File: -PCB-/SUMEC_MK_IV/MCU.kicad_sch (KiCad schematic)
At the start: 24 parts, among them J13 USB_TypeC, SW2 SW_Push, SW3 SW_Push, SW4 SW_Push, SW5 SW_Push, U3 ESP32-S3-WROOM-1, U4 USBLC6-2SC6

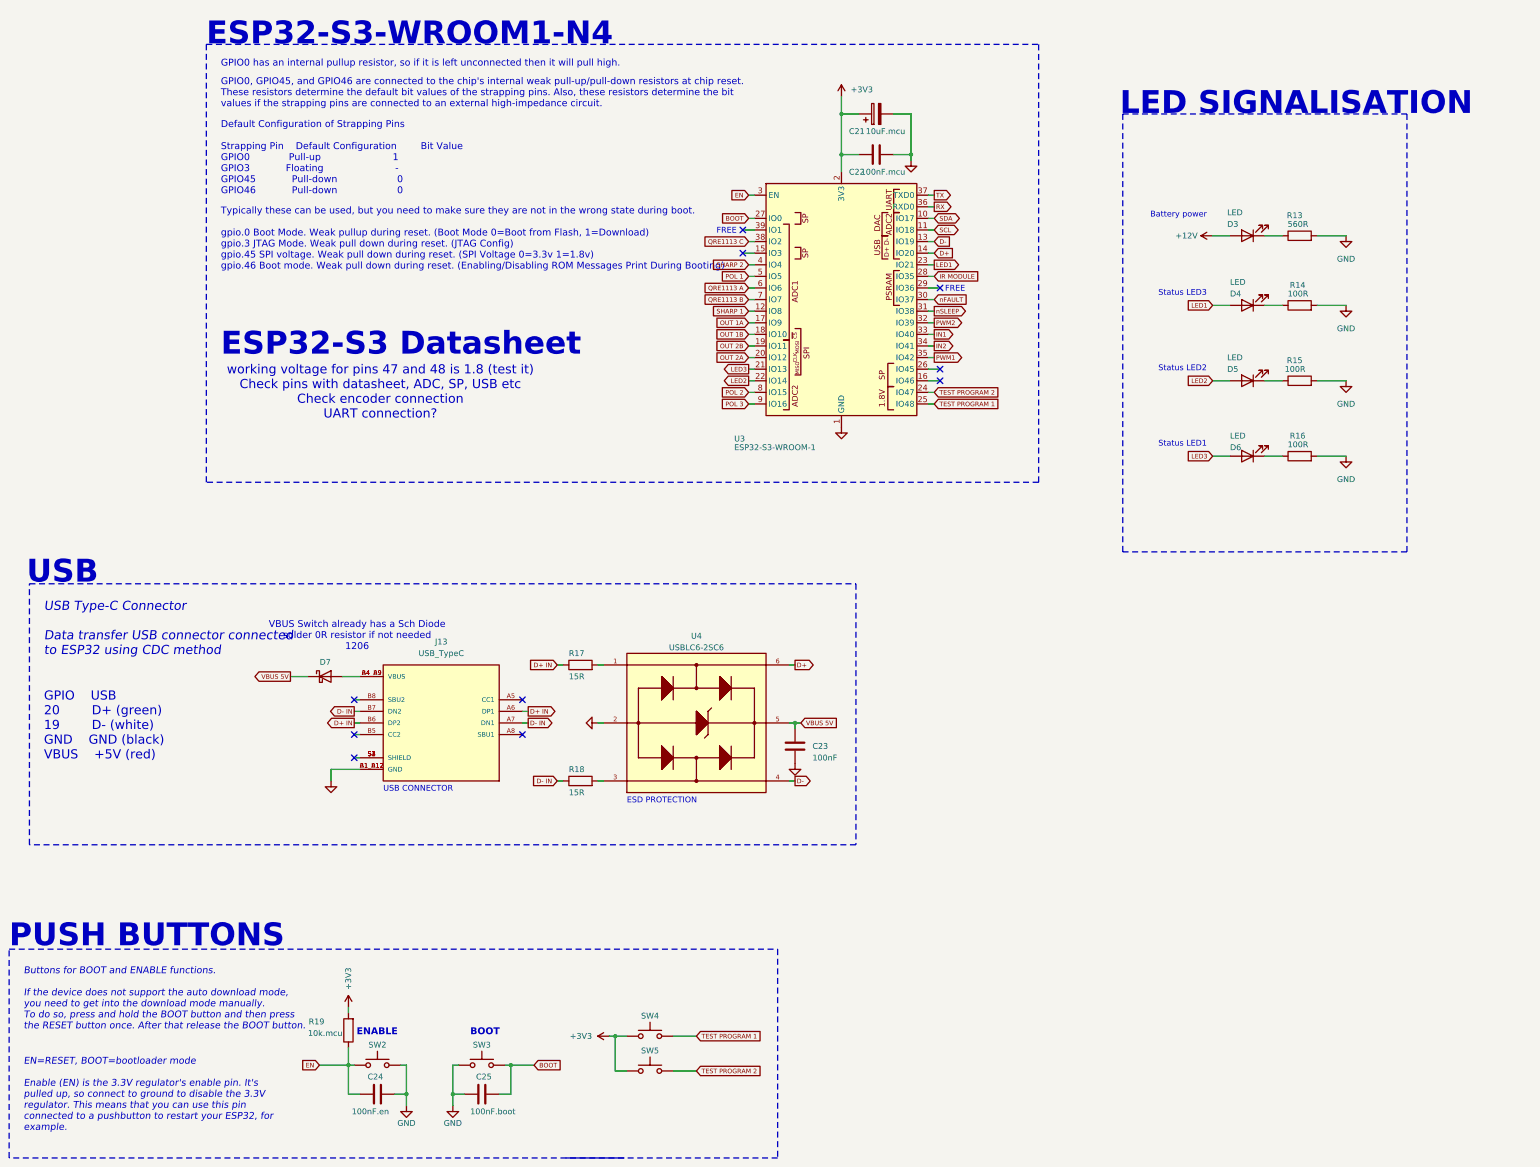
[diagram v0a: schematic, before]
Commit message: Schematic and PCB update
Schematic update:
- Font adjustment
- Block rearrangement

PCB update
- Silkscreen
- Minor layout update
- Graphic update
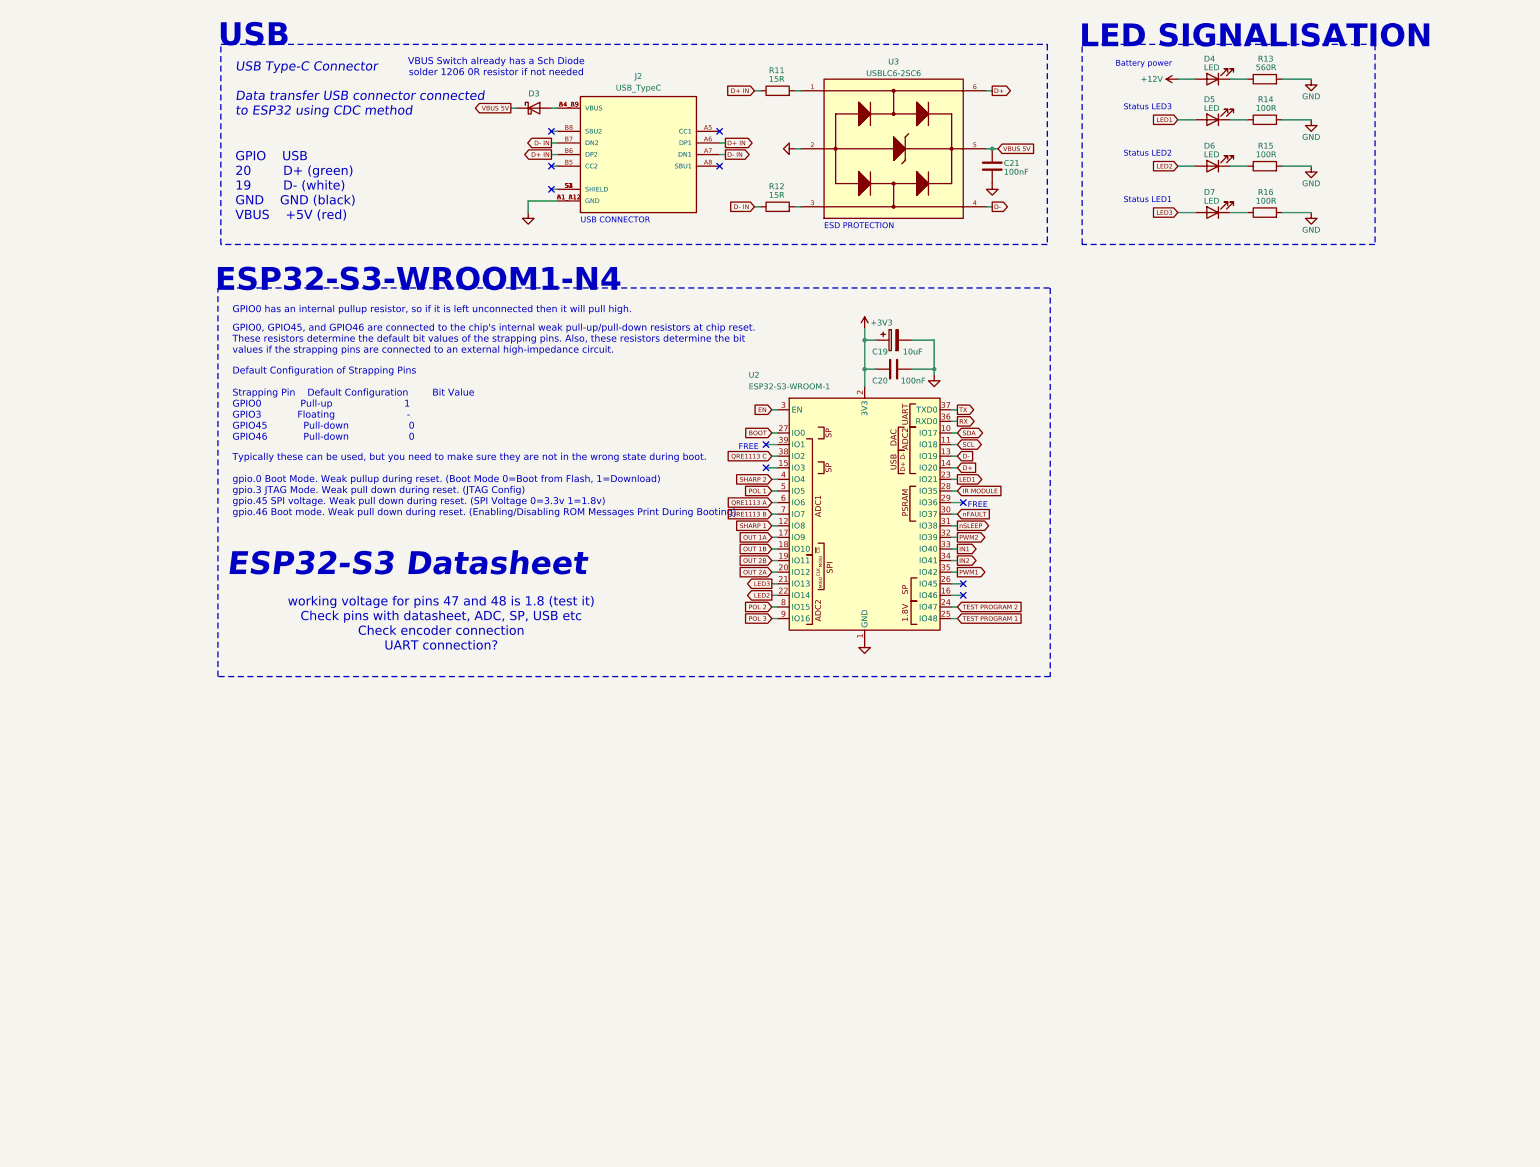
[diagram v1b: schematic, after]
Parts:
- removed C24: 100nF.en, Capacitor_SMD:C_0805_2012Metric_Pad1.18x1.45mm_HandSolder, symbol Device:C
- removed C25: 100nF.boot, Capacitor_SMD:C_0805_2012Metric_Pad1.18x1.45mm_HandSolder, symbol Device:C
- removed R19: 10k.mcu, Resistor_SMD:R_0805_2012Metric_Pad1.20x1.40mm_HandSolder, symbol Device:R
- removed SW2, SW3, SW4, SW5: SW_Push, Button_Switch_SMD:SW_SPST_EVQPE1, symbol Switch:SW_Push
- removed U3: ESP32-S3-WROOM-1, PCM_Espressif:ESP32-S3-WROOM-1, symbol sumec_sch_lib:ESP32-S3-WROOM-1_CUSTOM_made_by_bismarx
- added U2: ESP32-S3-WROOM-1, PCM_Espressif:ESP32-S3-WROOM-1, symbol sumec_sch_lib:ESP32-S3-WROOM-1_CUSTOM_made_by_bismarx
- C19: renamed from C21; value 10uF.mcu -> 10uF
- C20: renamed from C22; value 100nF.mcu -> 100nF
- renumbered C23 to C21, D7 to D3, D3 to D4, D4 to D5, D5 to D6, D6 to D7, J13 to J2, R17 to R11, R18 to R12, U4 to U3
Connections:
- net +3V3: now also U2.2 (3V3)
- net BOOT: now also U2.27 (IO0)
- net D+: now also U2.14 (IO20)
- net D-: now also U2.13 (IO19)
- net EN: now also U2.3 (EN)
- net GND: now also U2.1 (GND), U2.40 (GND), U2.41 (GND)
- net IN1: now also U2.33 (IO40)
- net IN2: now also U2.34 (IO41)
- net IR MODULE: now also U2.28 (IO35)
- net LED1: now also U2.23 (IO21)
- net LED2: now also U2.22 (IO14)
- net LED3: now also U2.21 (IO13)
- net OUT 1A: now also U2.17 (IO9)
- net OUT 1B: now also U2.18 (IO10)
- net OUT 2A: now also U2.20 (IO12)
- net OUT 2B: now also U2.19 (IO11)
- net POL 1: now also U2.5 (IO5)
- net POL 2: now also U2.8 (IO15)
- net POL 3: now also U2.9 (IO16)
- net PWM1: now also U2.35 (IO42)
- net PWM2: now also U2.32 (IO39)
- net QRE1113 A: now also U2.6 (IO6)
- net QRE1113 B: now also U2.7 (IO7)
- net QRE1113 C: now also U2.38 (IO2)
- net RX: now also U2.36 (RXD0)
- net SCL: now also U2.11 (IO18)
- net SDA: now also U2.10 (IO17)
- net SHARP 1: now also U2.12 (IO8)
- net SHARP 2: now also U2.4 (IO4)
- net TEST PROGRAM 1: now also U2.25 (IO48)
- net TEST PROGRAM 2: now also U2.24 (IO47)
- net TX: now also U2.37 (TXD0)
- net nFAULT: now also U2.30 (IO37)
- net nSLEEP: now also U2.31 (IO38)
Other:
- note added: "VBUS Switch already has a Sch Diode solder 1206 0R resistor if not needed"
- note removed: "BOOT"
- note removed: "Buttons for BOOT and ENABLE functions. If the device does not support the auto download mode, you need to get into the download mode manually. To do so, press and hold the BOOT button and then press the RESET button once. After that release the BOOT button."
- note removed: "EN=RESET, BOOT=bootloader mode Enable (EN) is the 3.3V regulator's enable pin. It's pulled up, so connect to ground to disable the 3.3V regulator. This means that you can use this pin connected to a pushbutton to restart your ESP32, for example."
- note removed: "ENABLE"
- note removed: "PUSH BUTTONS"
- note removed: "VBUS Switch already has a Sch Diode solder 0R resistor if not needed 1206"
- moved on the sheet: C19, C20, C21, D3, D4, D5, D6, D7, J2, R11, R12, R13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

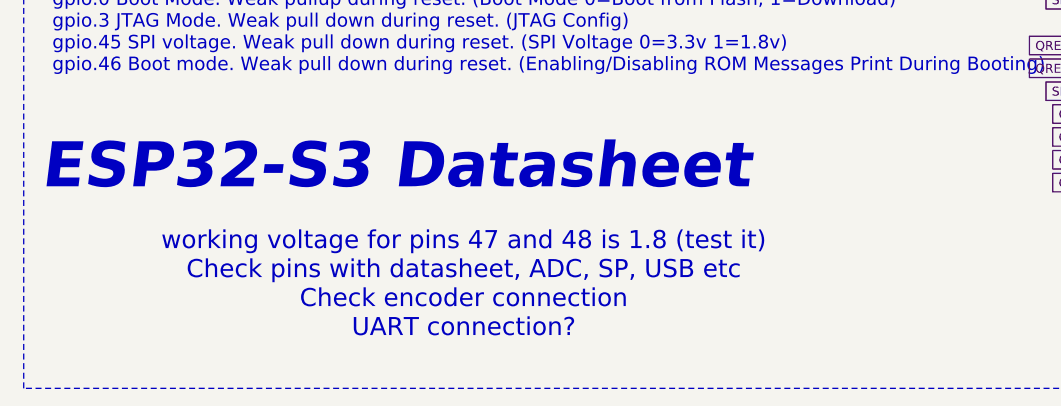
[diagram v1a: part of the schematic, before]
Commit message: silkscreen value rearrangement
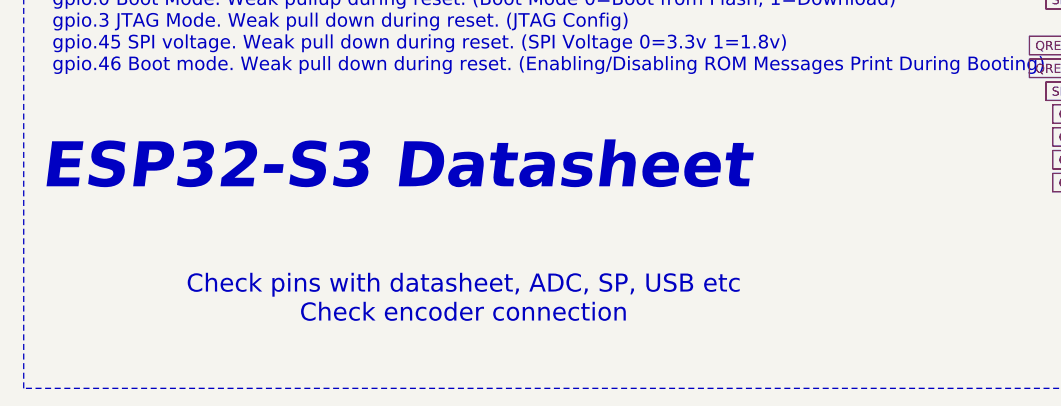
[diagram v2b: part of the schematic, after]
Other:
- note added: "Check pins with datasheet, ADC, SP, USB etc Check encoder connection"
- note removed: "working voltage for pins 47 and 48 is 1.8 (test it) Check pins with datasheet, ADC, SP, USB etc Check encoder connection UART connection?"
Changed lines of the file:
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@@
 		)
 	)
-	(text "working voltage for pins 47 and 48 is 1.8 (test it)\nCheck pins with datasheet, ADC, SP, USB etc\nCheck encoder connection\nUART connection?"
+	(text "\nCheck pins with datasheet, ADC, SP, USB etc\nCheck encoder connection"
 		(exclude_from_sim no)
 		(at 66.04 147.32 0)

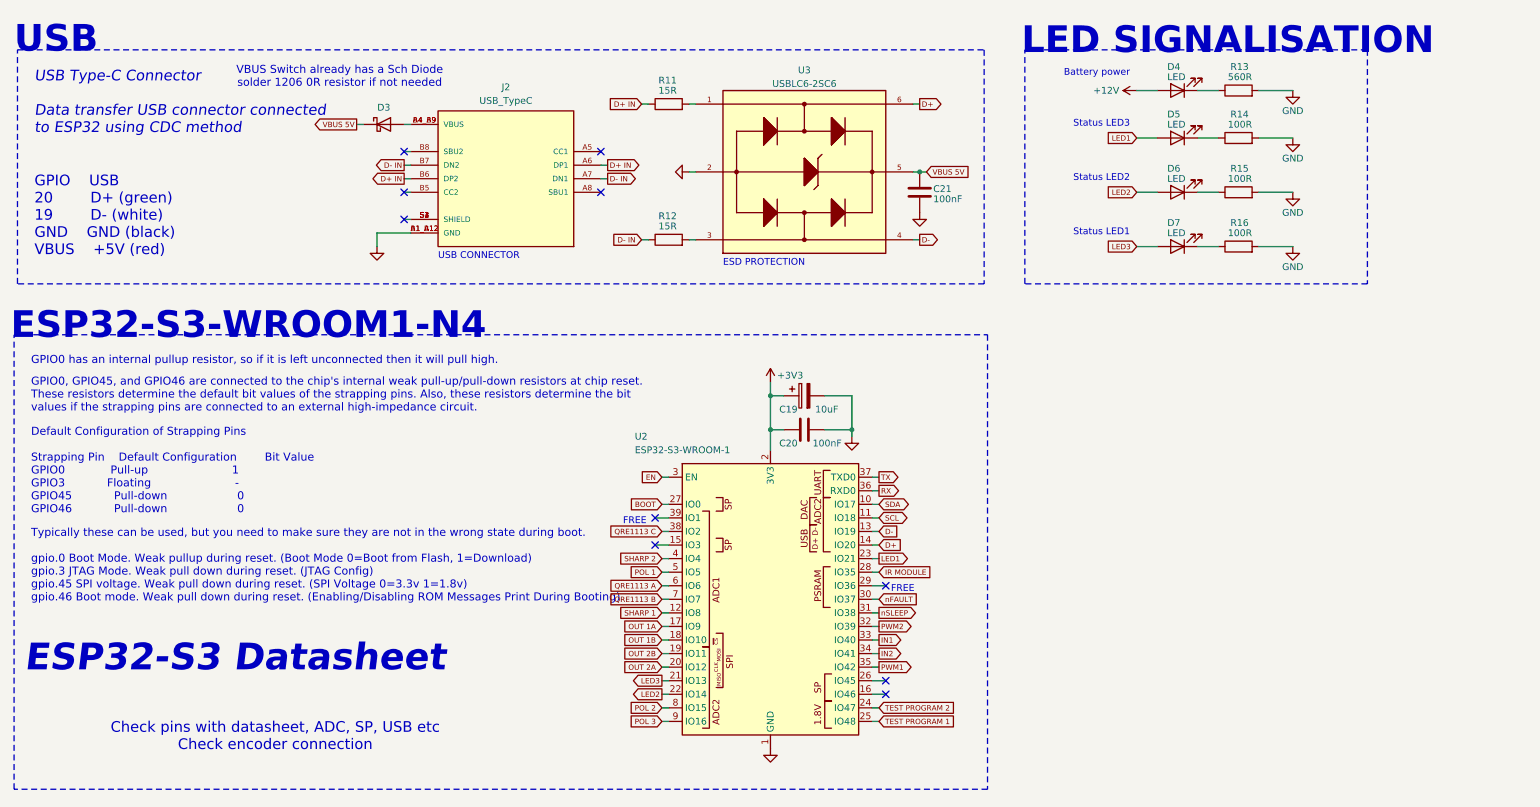
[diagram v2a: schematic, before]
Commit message: Board and schematic update.
PMOS switch added, 3d .step file created
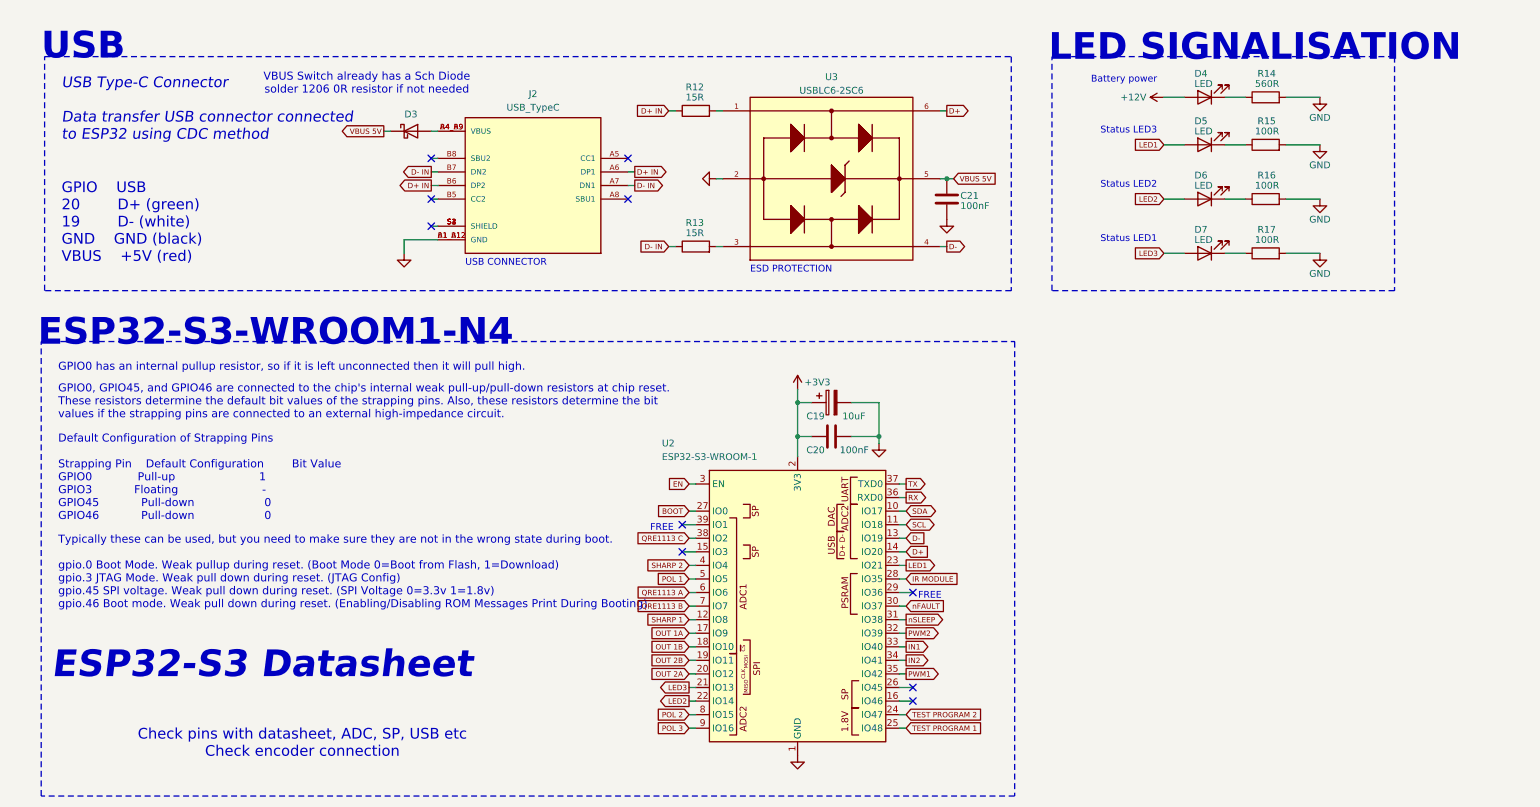
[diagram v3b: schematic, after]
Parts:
- renumbered R11 to R12, R12 to R13, R13 to R14, R14 to R15, R15 to R16, R16 to R17
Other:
- moved on the sheet: C19, C20, C21, D3, D4, D5, D6, D7, J2, R12, R13, R14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

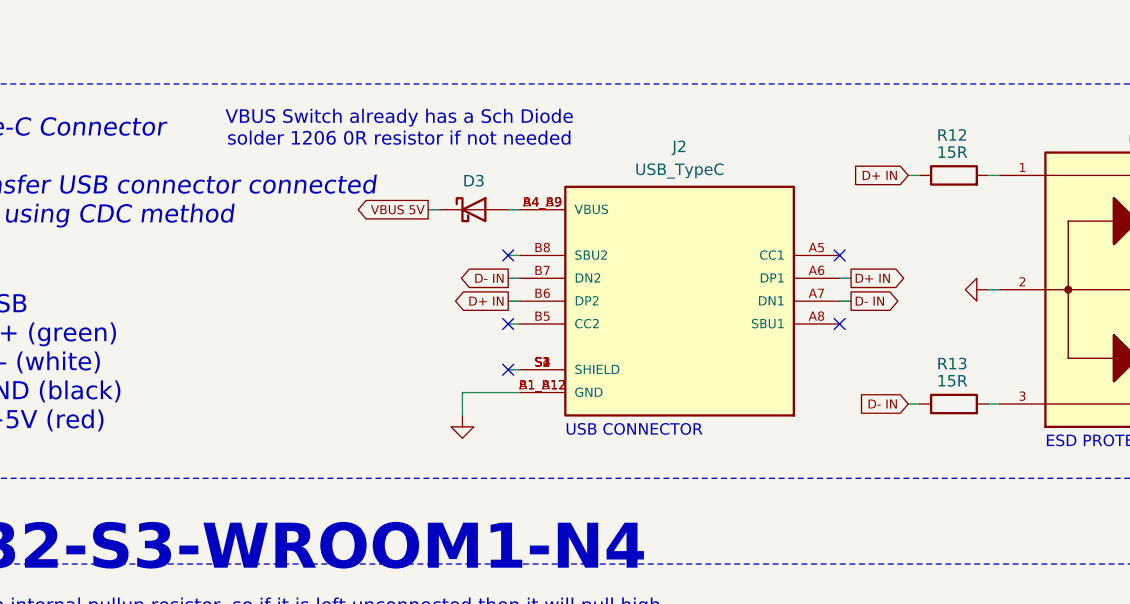
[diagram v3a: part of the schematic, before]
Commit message: Poly fuse over current protection
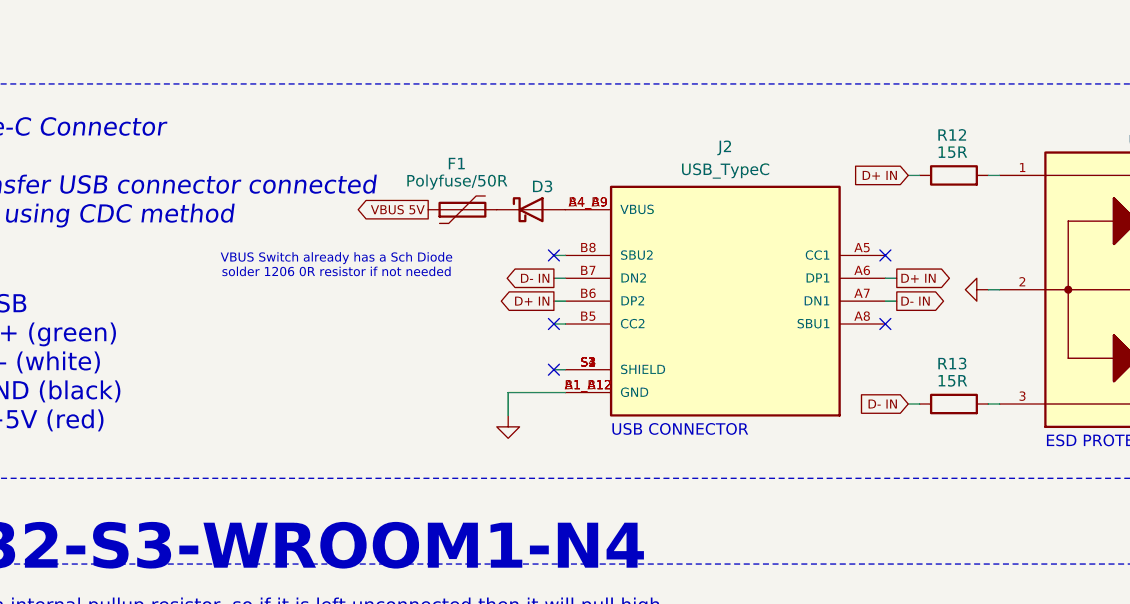
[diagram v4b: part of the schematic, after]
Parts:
- added F1: Polyfuse/50R, Fuse:Fuse_1206_3216Metric_Pad1.42x1.75mm_HandSolder, symbol Device:Polyfuse
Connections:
- net VBUS 5V: now also F1.1; no longer D3.1 (K)
- new net: D3.1 (K), F1.2
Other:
- moved on the sheet: D3, J2

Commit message: push buttons and some other shit
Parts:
- added C22, C23: 100nF, Capacitor_SMD:C_0805_2012Metric_Pad1.18x1.45mm_HandSolder, symbol Device:C
- added R14: 10k, Resistor_SMD:R_0805_2012Metric_Pad1.20x1.40mm_HandSolder, symbol Device:R
- added SW2, SW3, SW4, SW5: SW_Push, Button_Switch_SMD:SW_SPST_EVQPE1, symbol Switch:SW_Push
- renumbered R14 to R15, R15 to R16, R16 to R17, R17 to R18
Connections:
- net +3V3: now also R14.2, SW3.1, SW4.1
- net BOOT: now also C23.1, SW5.2
- net EN: now also C22.1, R14.1, SW2.2
- net GND: now also C22.2, C23.2, SW2.1, SW5.1
- net TEST PROGRAM 1: now also SW3.2
- net TEST PROGRAM 2: now also SW4.2
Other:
- note added: "BOOT"
- note added: "Buttons for BOOT and ENABLE functions. If the device does not support the auto download mode, you need to get into the download mode manually. To do so, press and hold the BOOT button and then press the RESET button once. After that release the BOOT button."
- note added: "EN=RESET, BOOT=bootloader mode Enable (EN) is the 3.3V regulator's enable pin. It's pulled up, so connect to ground to disable the 3.3V regulator. This means that you can use this pin connected to a pushbutton to restart your ESP32, for example."
- note added: "ENABLE"
- note added: "PUSH BUTTONS"
